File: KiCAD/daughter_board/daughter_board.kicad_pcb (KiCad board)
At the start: 2 copper layers, 41 x 33 mm, 29 parts, among them IC1 QMC5883L, J1 JST, J3 SM02B-SRSS-TB_LF__SN_, U1 TPS61023DRLR, U2 SN74AHCT1G125DBVR, U3 XIAO-ESP32-C3-SMD, U4 MPU-6050

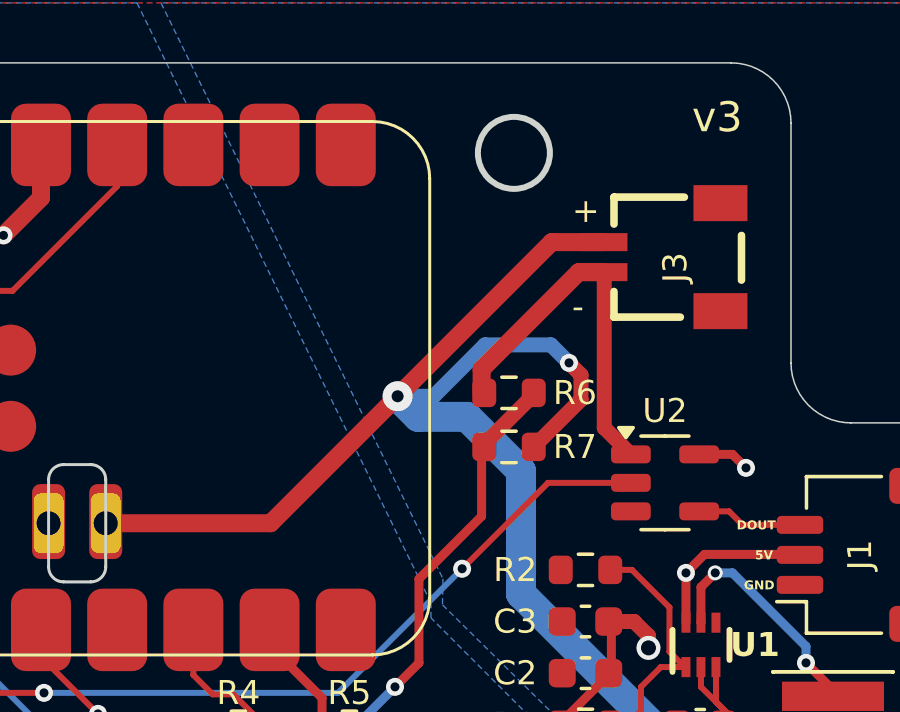
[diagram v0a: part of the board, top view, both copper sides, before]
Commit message: reversed the polatrity of the power plug in the daughter board
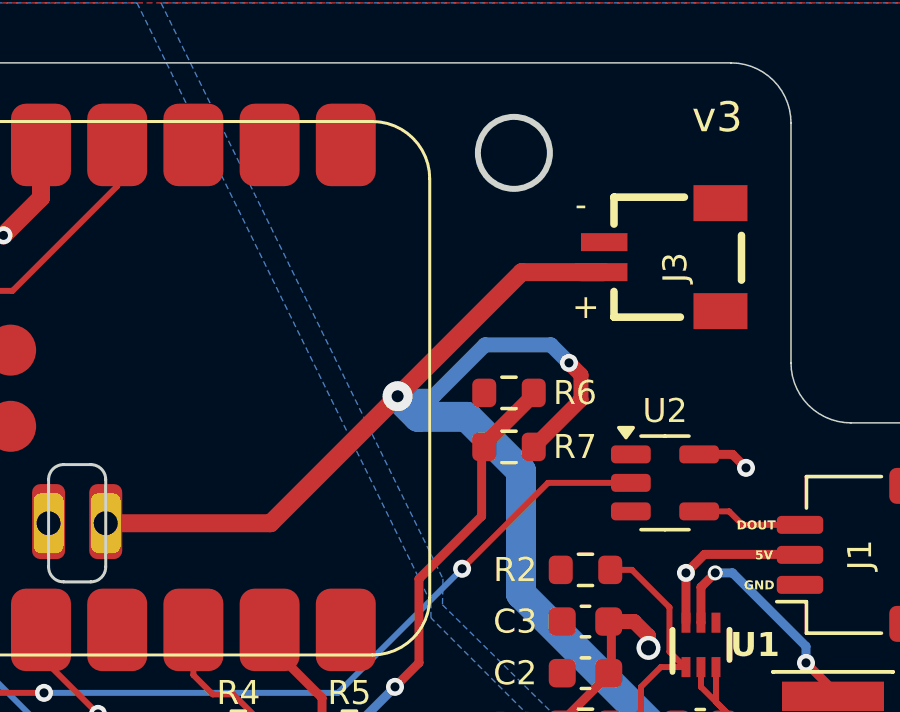
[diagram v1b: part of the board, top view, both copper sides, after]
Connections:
- J3 pad 1: -BATT -> +BATT
- J3 pad 2: +BATT -> -BATT
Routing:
- net -BATT: track 18.8 -> 6.10 mm
